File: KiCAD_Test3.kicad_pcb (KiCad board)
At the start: 2 copper layers, 58.7 x 53.7 mm, 43 parts, among them J1 HDR_6_2.54, P1 PCIEx4 EDGE CONNECTOR, U1 ESP32-D0WDQ6, U2 TXB0104PWR, U3 IS25WP032D

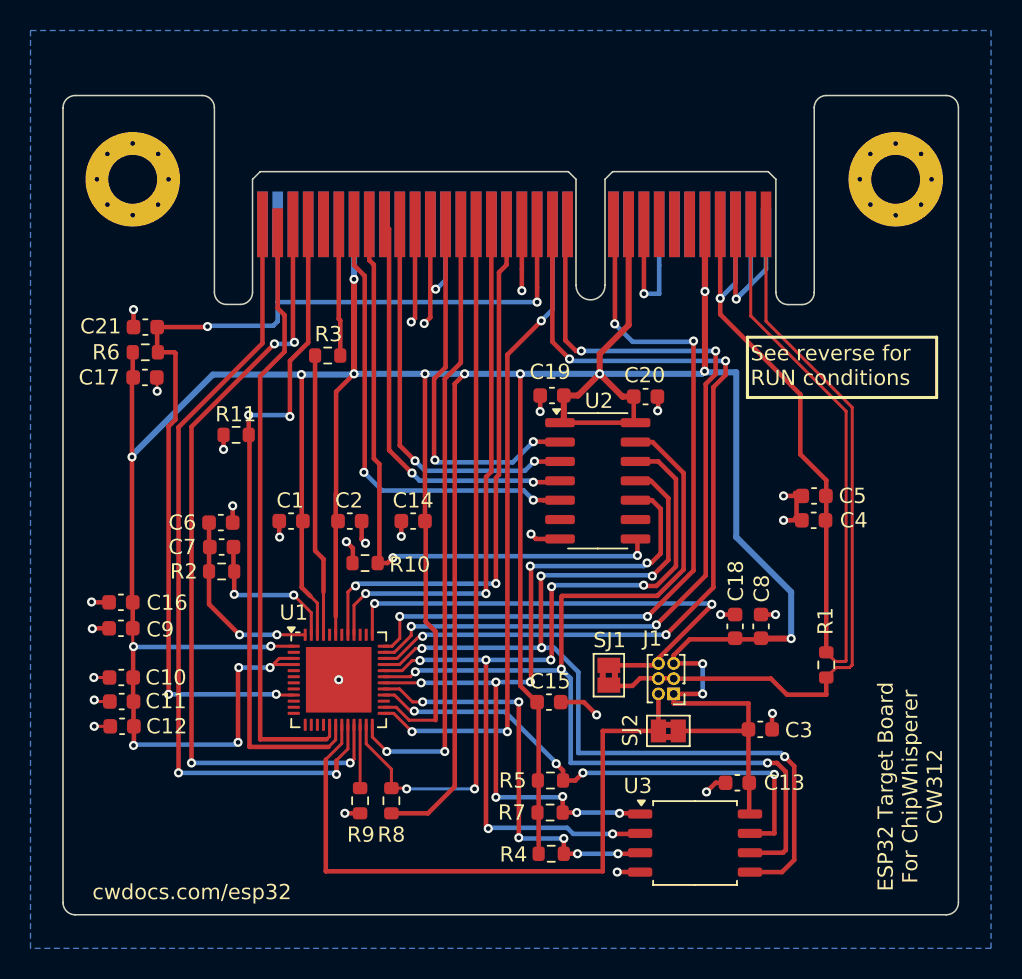
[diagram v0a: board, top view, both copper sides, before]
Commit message: updated pcb and schematic after library re-organization, also updated header to the correct footprint
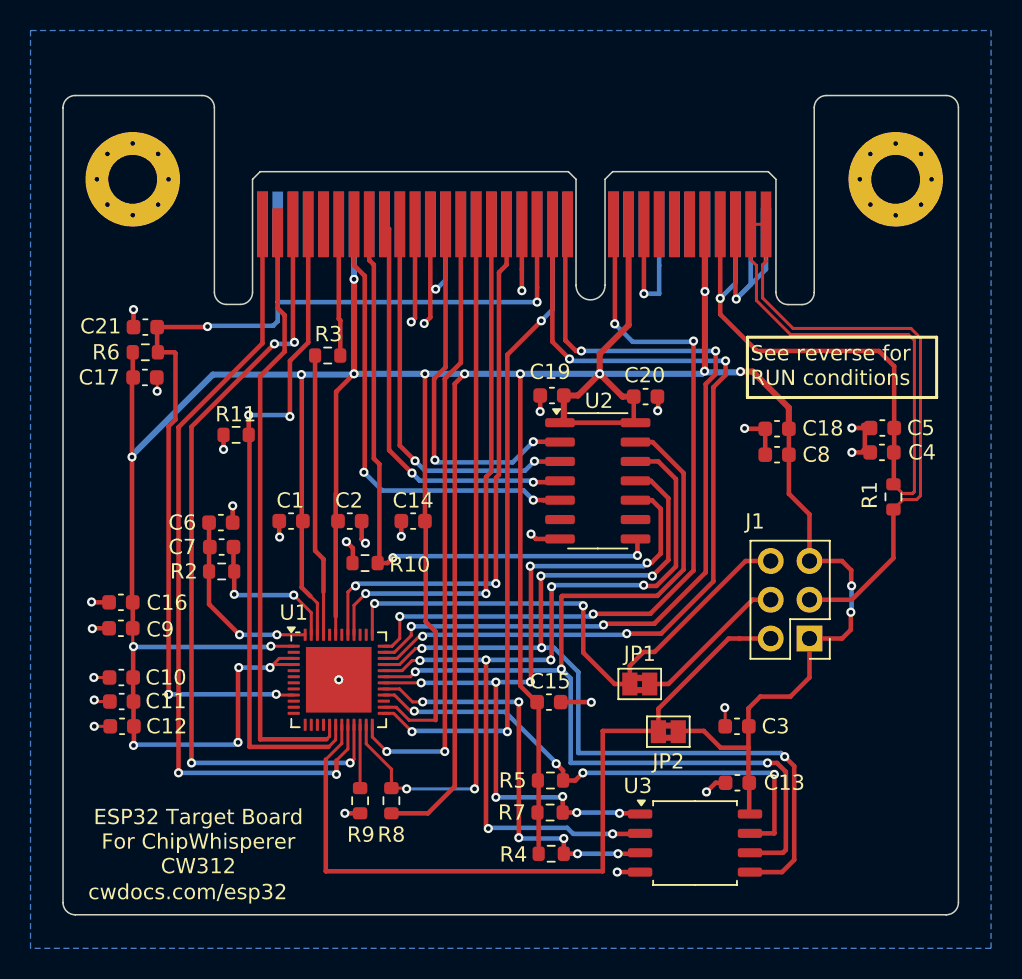
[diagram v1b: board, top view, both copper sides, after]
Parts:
- removed SJ1, SJ2: ~, Jumper:SolderJumper-2_P1.3mm_Bridged2Bar_Pad1.0x1.5mm
- added JP1: ~, Jumper:SolderJumper-2_P1.3mm_Bridged2Bar_Pad1.0x1.5mm, F.Cu at (162.3, 104.2)
- added JP2: ~, Jumper:SolderJumper-2_P1.3mm_Bridged2Bar_Pad1.0x1.5mm, F.Cu at (164.1, 107.3)
- J1: footprint Connector_PinHeader_1.00mm:PinHeader_2x03_P1.00mm_Vertical -> Connector_PinHeader_2.54mm:PinHeader_2x03_P2.54mm_Vertical
- moved C18 13.2 mm to (171.3, 87.5), turned to 180 degrees
- moved R1 11.9 mm to (178.9, 91.9)
- moved C8 11.3 mm to (171.3, 89.2), turned to 180 degrees
- moved J1 9.61 mm to (173.4, 101.2)
- moved C5 6.31 mm to (178.2, 87.4)
- moved C4 6.31 mm to (178.2, 89.0)
- moved PCB4 5.06 mm to (177.0, 90.0)
- moved C3 1.54 mm to (168.7, 107.0), turned to 180 degrees
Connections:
- C4 pad 1: /Connector/SHUNTH -> /Connector/SHUNTL
- C5 pad 1: /Connector/SHUNTH -> /Connector/SHUNTL
- J1 pad 4: /Connector/SHUNTL -> Net-(J1-Pad4)
- P1 pad A3: /Connector/SHUNTH -> /Connector/SHUNTL
- P1 pad B2: /Connector/SHUNTH -> /Connector/SHUNTL
- P1 pad B4: /Connector/SHUNTH -> /Connector/SHUNTL
- R1 pad 2: /Connector/SHUNTH -> /Connector/SHUNTL
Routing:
- net /Connector/SHUNTH: track 69.2 -> 0.00 mm, vias 1 -> 0
- net /Connector/SHUNTL: track 49.3 -> 99.8 mm, vias 0 -> 1
- net Net-(J1-Pad4): track 0.00 -> 10.2 mm
- net /Integrated_Circuits/VDD RTC: track 43.5 -> 51.8 mm
- net VCC: track 326.9 -> 320.2 mm
- net /Integrated_Circuits/VDD CPU: track 32.9 -> 36.2 mm
- net GND: track 81.1 -> 82.0 mm, vias 32 -> 31
